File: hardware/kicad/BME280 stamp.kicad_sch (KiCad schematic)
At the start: 7 parts, among them U1 BME280

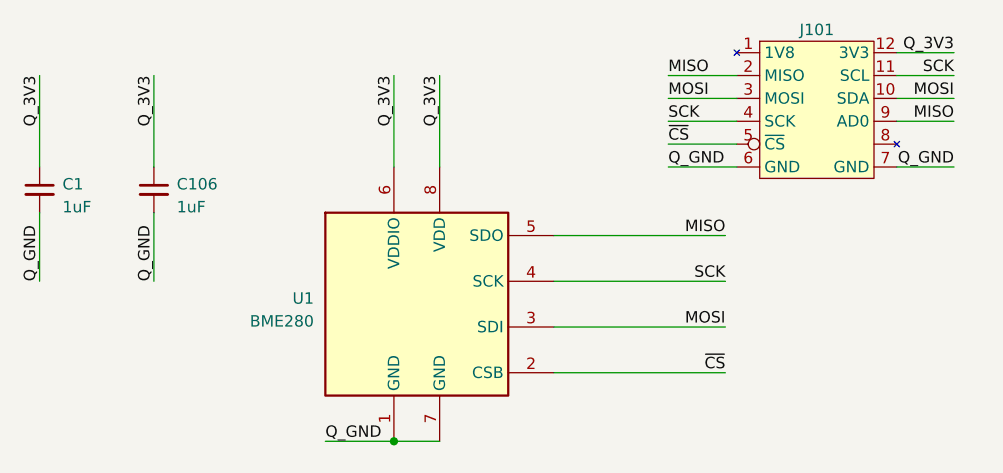
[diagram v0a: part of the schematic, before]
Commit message: Imported shipometer hat 23.04 as built, updated to Kicad 9
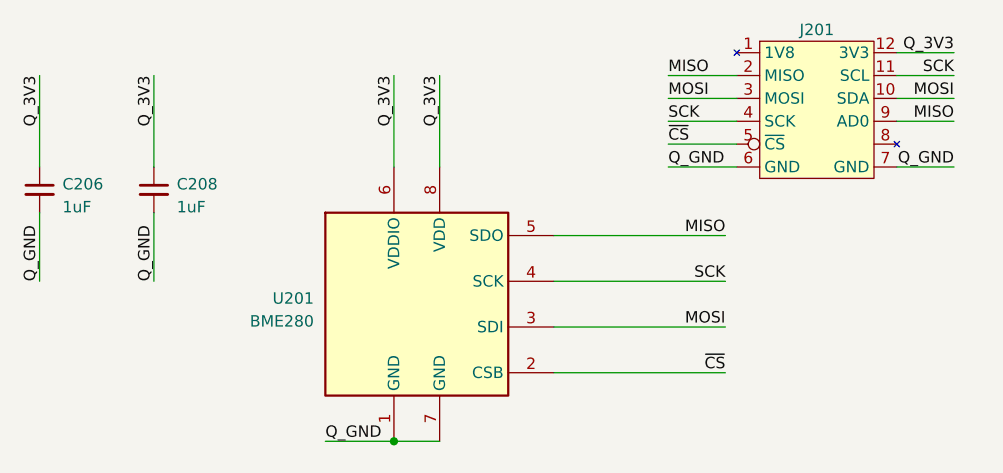
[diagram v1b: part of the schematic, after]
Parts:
- renumbered C1 to C206, C106 to C208, G1 to G201, G2 to G202, G3 to G203, J101 to J201, U1 to U201
